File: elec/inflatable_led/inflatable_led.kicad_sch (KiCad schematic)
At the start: 103 parts, among them CN1 S2B-PH-SM4-TB(LF)(SN), J1 Conn_01x10, J2 Conn_01x02_Pin, J3 Conn_01x02_Pin, J4 USB4205-GF-A_REVA, Q1 2N7002KW_R1_00001, U1 RP2040, U2 W25Q128JVSIQTR, U3 TPS61165DRVR, U4 BQ25601DRTWR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

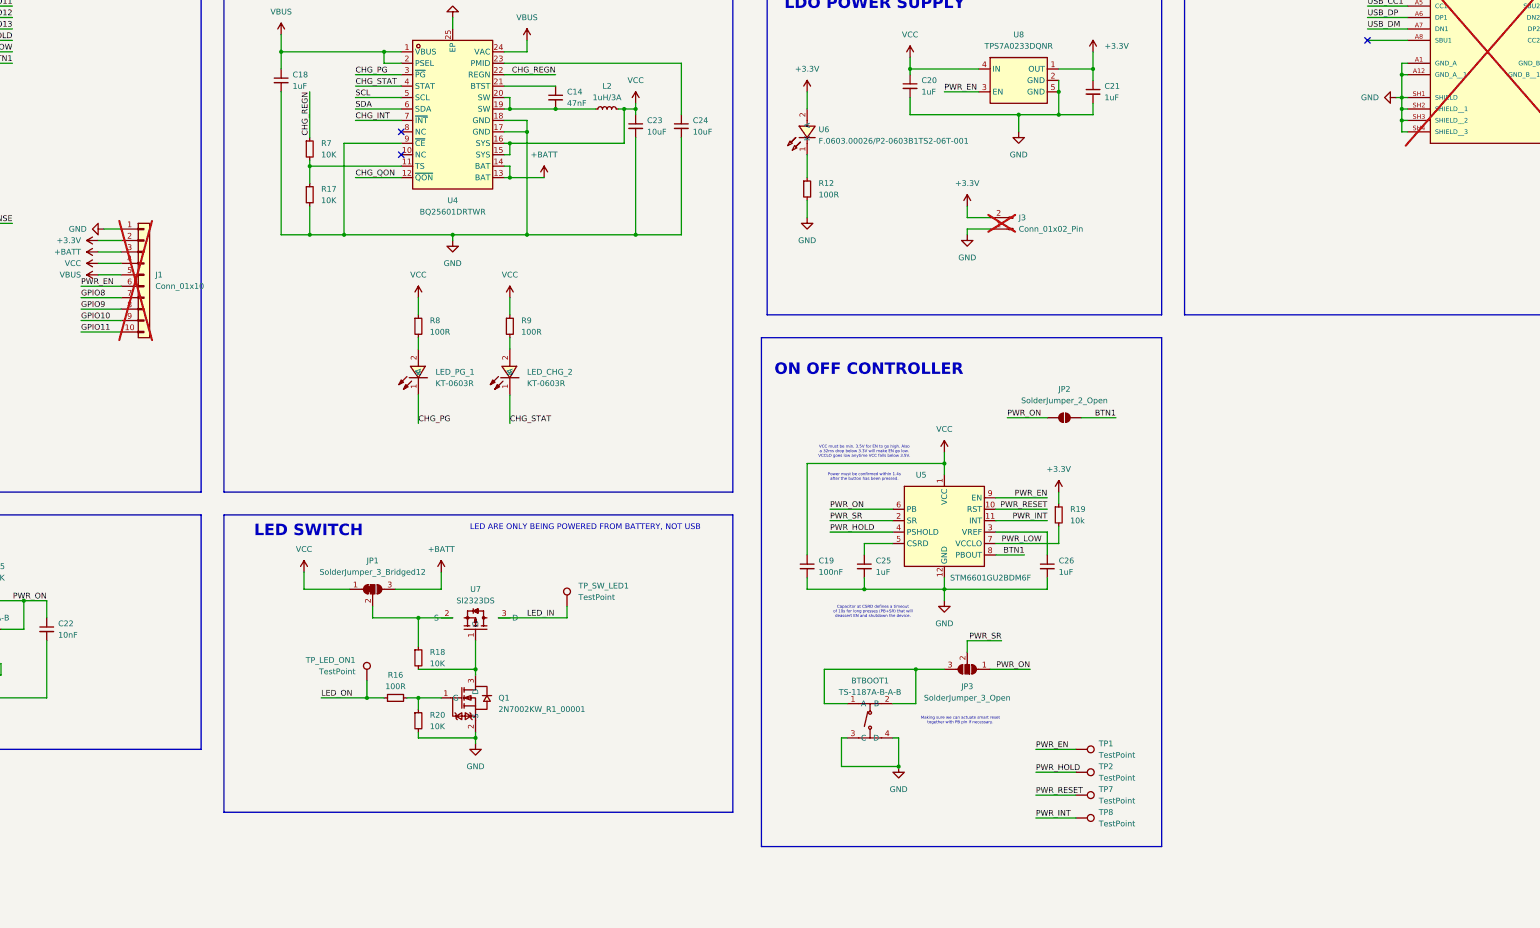
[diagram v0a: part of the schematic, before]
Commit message: add OR gate to circuit
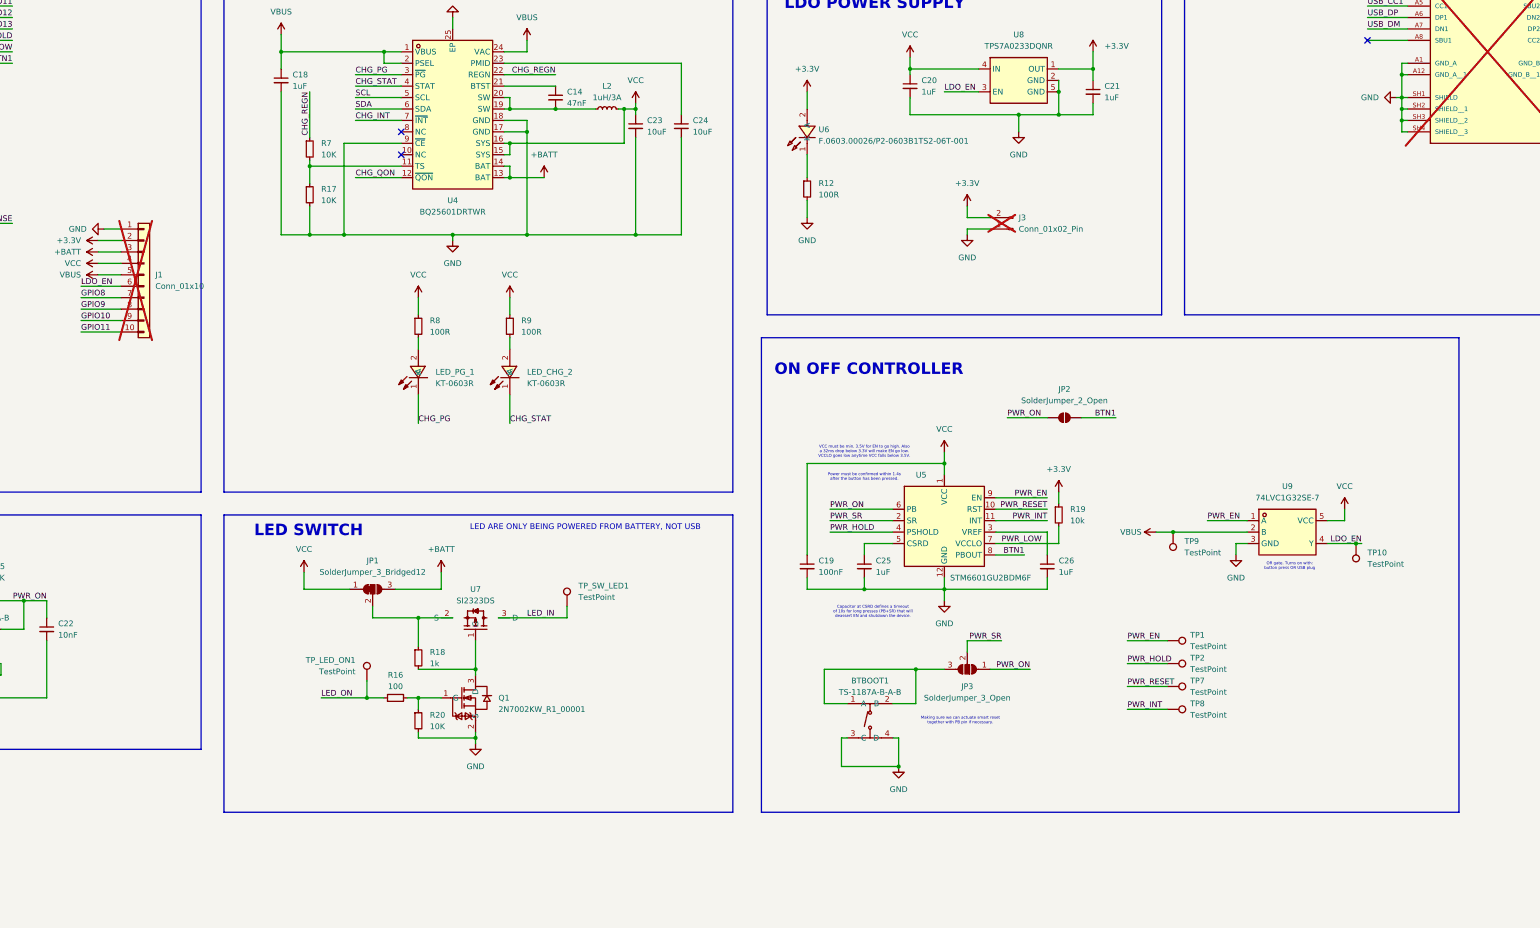
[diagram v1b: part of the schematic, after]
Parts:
- added TP10, TP9: TestPoint, TestPoint:TestPoint_Pad_D1.0mm, symbol Connector:TestPoint
- added U9: 74LVC1G32SE-7, footprints:SOT-353_L2.0-W1.2-P0.65-LS2.1-BL, symbol local:74LVC1G32SE-7
- R16: value 100R -> 100
- R18: value 10K -> 1k; LCSC Part C25744 -> C11702
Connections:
- net GND: now also U9.3 (GND)
- net PWR_EN: now also U9.1 (A); no longer J1.6 (Pin_6), U8.3 (EN)
- net VBUS: now also TP9.1, U9.2 (B)
- net VCC: now also U9.5 (VCC)
- new net LDO_EN: J1.6 (Pin_6), TP10.1, U8.3 (EN), U9.4 (Y)
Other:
- note added: "OR gate. Turns on with: button press OR USB plug"
- moved on the sheet: TP1, TP2, TP7, TP8
